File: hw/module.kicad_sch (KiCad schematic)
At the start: 7 parts

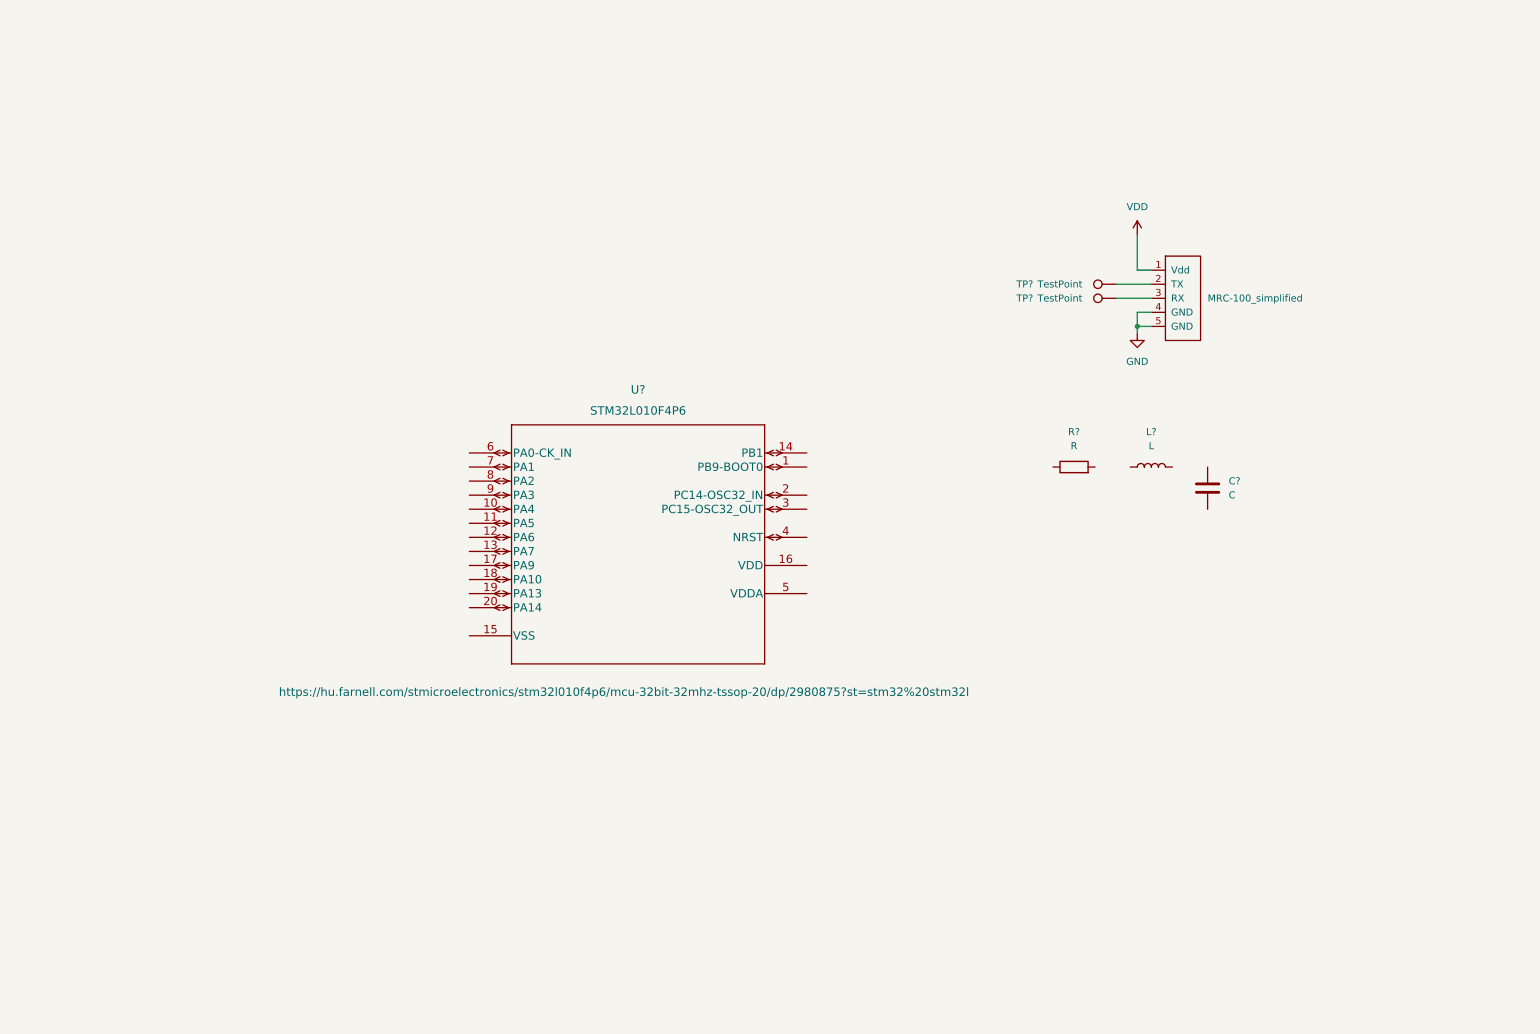
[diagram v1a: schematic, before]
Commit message: added Max919_footprint
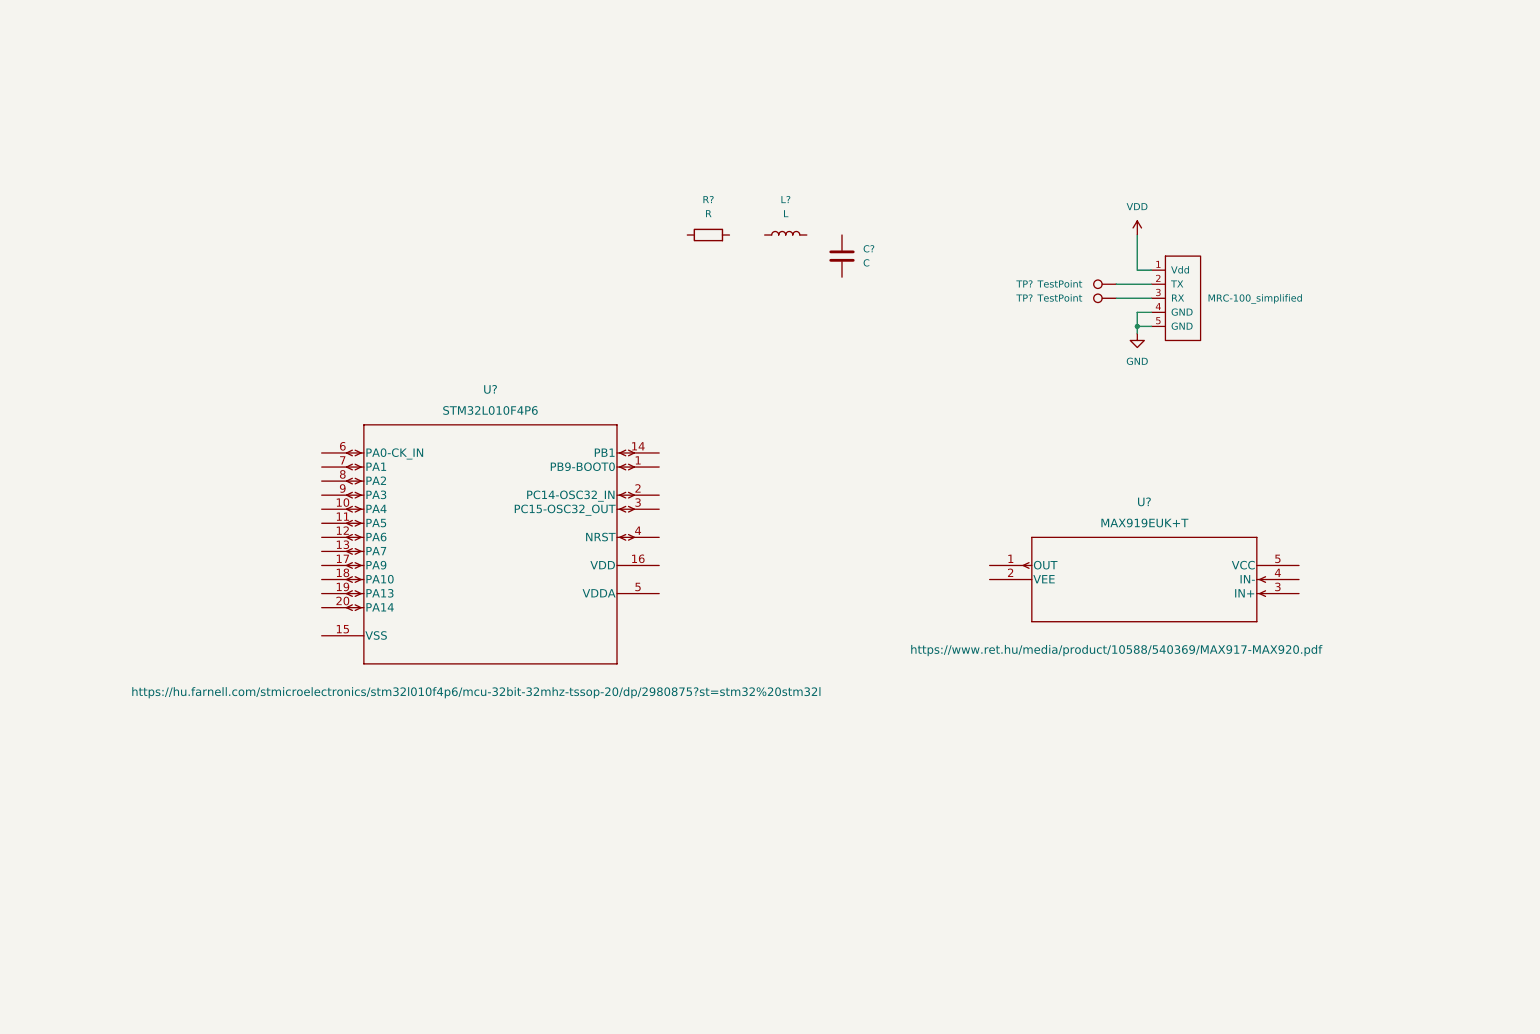
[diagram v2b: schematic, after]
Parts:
- added U?: MAX919EUK+T, max919:MAX919EUK&plus_T, symbol max919:MAX919EUK+T
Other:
- moved on the sheet: C?, L?, R?, U?
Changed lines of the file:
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@@
     (pin "1")
   )
-  (symbol (lib_id "Device:L") (at 210.82 95.25 90) (unit 1)
+  (symbol (lib_id "Device:L") (at 144.78 53.34 90) (unit 1)
     (in_bom yes) (on_board yes) (fields_autoplaced)
-    (property "Reference" "L?" (id 0) (at 210.82 88.9 90))
-    (property "Value" "L" (id 1) (at 210.82 91.44 90))
-    (property "Footprint" "" (id 2) (at 210.82 95.25 0)
+    (property "Reference" "L?" (id 0) (at 144.78 46.99 90))
+    (property "Value" "L" (id 1) (at 144.78 49.53 90))
+    (property "Footprint" "" (id 2) (at 144.78 53.34 0)
       (effects (font (size 1.27 1.27)) hide)
     )
-    (property "Datasheet" "~" (id 3) (at 210.82 95.25 0)
+    (property "Datasheet" "~" (id 3) (at 144.78 53.34 0)
       (effects (font (size 1.27 1.27)) hide)
     )
@@
     (pin "2")
   )
-  (symbol (lib_id "Device:R") (at 196.85 95.25 90) (unit 1)
+  (symbol (lib_id "Device:R") (at 130.81 53.34 90) (unit 1)
     (in_bom yes) (on_board yes) (fields_autoplaced)
-    (property "Reference" "R?" (id 0) (at 196.85 88.9 90))
-    (property "Value" "R" (id 1) (at 196.85 91.44 90))
-    (property "Footprint" "" (id 2) (at 196.85 97.028 90)
+    (property "Reference" "R?" (id 0) (at 130.81 46.99 90))
+    (property "Value" "R" (id 1) (at 130.81 49.53 90))
+    (property "Footprint" "" (id 2) (at 130.81 55.118 90)
       (effects (font (size 1.27 1.27)) hide)
     )
-    (property "Datasheet" "~" (id 3) (at 196.85 95.25 0)
+    (property "Datasheet" "~" (id 3) (at 130.81 53.34 0)
       (effects (font (size 1.27 1.27)) hide)
     )
@@
     (pin "1")
   )
-  (symbol (lib_id "farnell:STM32L010F4P6") (at 87.63 92.71 0) (unit 1)
+  (symbol (lib_id "max919:MAX919EUK+T") (at 181.61 113.03 0) (unit 1)
     (in_bom yes) (on_board yes)
-    (property "Reference" "U?" (id 0) (at 118.11 81.28 0)
+    (property "Reference" "U?" (id 0) (at 209.55 101.6 0)
       (effects (font (size 1.524 1.524)))
     )
-    (property "Value" "STM32L010F4P6" (id 1) (at 118.11 85.09 0)
+    (property "Value" "MAX919EUK+T" (id 1) (at 209.55 105.41 0)
       (effects (font (size 1.524 1.524)))
     )
-    (property "Footprint" "farnell:STM32L010F4P6" (id 2) (at 118.11 86.614 0)
+    (property "Footprint" "max919:MAX919EUK&plus_T" (id 2) (at 209.55 106.934 0)
       (effects (font (size 1.524 1.524)) hide)
     )
-    (property "Datasheet" "https://hu.farnell.com/stmicroelectronics/stm32l010f4p6/mcu-32bit-32mhz-tssop-20/dp/2980875?st=stm32%20stm32l" (id 3) (at 115.57 135.89 0)
+    (property "Datasheet" "https://www.ret.hu/media/product/10588/540369/MAX917-MAX920.pdf" (id 3) (at 204.47 128.27 0)
+      (effects (font (size 1.524 1.524)))
+    )
+    (pin "1")
+    (pin "2")
+    (pin "3")
+    (pin "4")
+    (pin "5")
+  )
+  (symbol (lib_id "farnell:STM32L010F4P6") (at 60.96 92.71 0) (unit 1)
+    (in_bom yes) (on_board yes)
+    (property "Reference" "U?" (id 0) (at 91.44 81.28 0)
+      (effects (font (size 1.524 1.524)))
+    )
+    (property "Value" "STM32L010F4P6" (id 1) (at 91.44 85.09 0)
+      (effects (font (size 1.524 1.524)))
+    )
+    (property "Footprint" "farnell:STM32L010F4P6" (id 2) (at 91.44 86.614 0)
+      (effects (font (size 1.524 1.524)) hide)
+    )
+    (property "Datasheet" "https://hu.farnell.com/stmicroelectronics/stm32l010f4p6/mcu-32bit-32mhz-tssop-20/dp/2980875?st=stm32%20stm32l" (id 3) (at 88.9 135.89 0)
       (effects (font (size 1.524 1.524)))
     )
@@
     (pin "9")
   )
-  (symbol (lib_id "Device:C") (at 220.98 99.06 0) (unit 1)
+  (symbol (lib_id "Device:C") (at 154.94 57.15 0) (unit 1)
     (in_bom yes) (on_board yes) (fields_autoplaced)
-    (property "Reference" "C?" (id 0) (at 224.79 97.7899 0)
+    (property "Reference" "C?" (id 0) (at 158.75 55.8799 0)
       (effects (font (size 1.27 1.27)) (justify left))
     )
-    (property "Value" "C" (id 1) (at 224.79 100.3299 0)
+    (property "Value" "C" (id 1) (at 158.75 58.4199 0)
       (effects (font (size 1.27 1.27)) (justify left))
     )
-    (property "Footprint" "" (id 2) (at 221.9452 102.87 0)
+    (property "Footprint" "" (id 2) (at 155.9052 60.96 0)
       (effects (font (size 1.27 1.27)) hide)
     )
-    (property "Datasheet" "~" (id 3) (at 220.98 99.06 0)
+    (property "Datasheet" "~" (id 3) (at 154.94 57.15 0)
       (effects (font (size 1.27 1.27)) hide)
     )
@@
       (reference "TP?") (unit 1) (value "TestPoint") (footprint "TestPoint:TestPoint_Pad_3.0x3.0mm")
     )
+    (path "/b184c922-aa81-4212-9d5b-fb2052d1a7d8"
+      (reference "U?") (unit 1) (value "MAX919EUK+T") (footprint "max919:MAX919EUK&plus_T")
+    )
     (path "/c3a09ed2-f9ee-4187-a81e-7663ad390909"

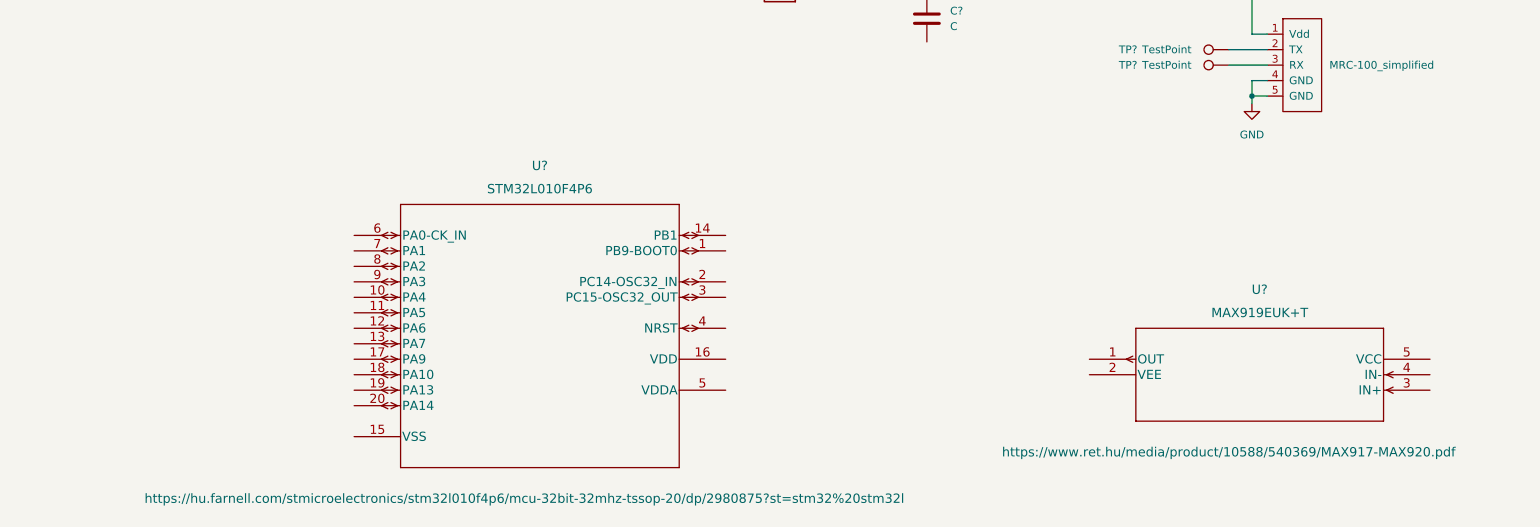
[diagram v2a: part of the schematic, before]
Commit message: Redraw max919 to conventional symbol
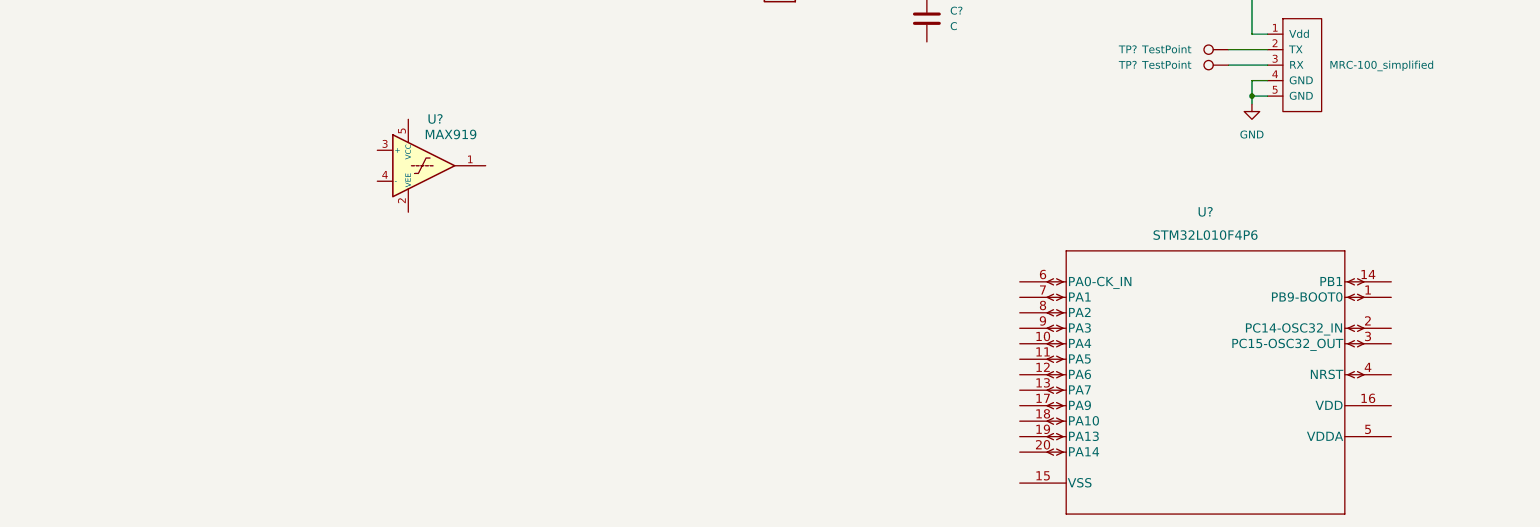
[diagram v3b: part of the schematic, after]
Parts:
- removed U?: MAX919EUK+T, max919:MAX919EUK&plus_T, symbol max919:MAX919EUK+T
- added U?: MAX919, Package_TO_SOT_SMD:SOT-23-5_HandSoldering, symbol RET:MAX919
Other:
- moved on the sheet: U?
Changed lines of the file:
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@@
     (pin "1")
   )
-  (symbol (lib_id "max919:MAX919EUK+T") (at 181.61 113.03 0) (unit 1)
+  (symbol (lib_id "farnell:STM32L010F4P6") (at 170.18 100.33 0) (unit 1)
     (in_bom yes) (on_board yes)
-    (property "Reference" "U?" (id 0) (at 209.55 101.6 0)
+    (property "Reference" "U?" (id 0) (at 200.66 88.9 0)
       (effects (font (size 1.524 1.524)))
     )
-    (property "Value" "MAX919EUK+T" (id 1) (at 209.55 105.41 0)
+    (property "Value" "STM32L010F4P6" (id 1) (at 200.66 92.71 0)
       (effects (font (size 1.524 1.524)))
     )
-    (property "Footprint" "max919:MAX919EUK&plus_T" (id 2) (at 209.55 106.934 0)
+    (property "Footprint" "farnell:STM32L010F4P6" (id 2) (at 200.66 94.234 0)
       (effects (font (size 1.524 1.524)) hide)
     )
-    (property "Datasheet" "https://www.ret.hu/media/product/10588/540369/MAX917-MAX920.pdf" (id 3) (at 204.47 128.27 0)
-      (effects (font (size 1.524 1.524)))
-    )
-    (pin "1")
-    (pin "2")
-    (pin "3")
-    (pin "4")
-    (pin "5")
-  )
-  (symbol (lib_id "farnell:STM32L010F4P6") (at 60.96 92.71 0) (unit 1)
-    (in_bom yes) (on_board yes)
-    (property "Reference" "U?" (id 0) (at 91.44 81.28 0)
-      (effects (font (size 1.524 1.524)))
-    )
-    (property "Value" "STM32L010F4P6" (id 1) (at 91.44 85.09 0)
-      (effects (font (size 1.524 1.524)))
-    )
-    (property "Footprint" "farnell:STM32L010F4P6" (id 2) (at 91.44 86.614 0)
+    (property "Datasheet" "https://hu.farnell.com/stmicroelectronics/stm32l010f4p6/mcu-32bit-32mhz-tssop-20/dp/2980875?st=stm32%20stm32l" (id 3) (at 198.12 143.51 0)
       (effects (font (size 1.524 1.524)) hide)
-    )
-    (property "Datasheet" "https://hu.farnell.com/stmicroelectronics/stm32l010f4p6/mcu-32bit-32mhz-tssop-20/dp/2980875?st=stm32%20stm32l" (id 3) (at 88.9 135.89 0)
-      (effects (font (size 1.524 1.524)))
     )
     (pin "1")
@@
     (pin "2")
   )
+  (symbol (lib_id "RET:MAX919") (at 71.12 81.28 0) (unit 1)
+    (in_bom yes) (on_board yes)
+    (property "Reference" "U?" (id 0) (at 74.295 73.66 0)
+      (effects (font (size 1.524 1.524)))
+    )
+    (property "Value" "MAX919" (id 1) (at 76.835 76.2 0)
+      (effects (font (size 1.524 1.524)))
+    )
+    (property "Footprint" "Package_TO_SOT_SMD:SOT-23-5_HandSoldering" (id 2) (at 81.28 77.47 0)
+      (effects (font (size 1.524 1.524)) hide)
+    )
+    (property "Datasheet" "https://www.ret.hu/media/product/10588/540369/MAX917-MAX920.pdf" (id 3) (at 82.55 92.71 0)
+      (effects (font (size 1.524 1.524)) hide)
+    )
+    (pin "1")
+    (pin "2")
+    (pin "3")
+    (pin "4")
+    (pin "5")
+  )
   (sheet_instances
     (path "/" (page "1"))
@@
       (reference "TP?") (unit 1) (value "TestPoint") (footprint "TestPoint:TestPoint_Pad_3.0x3.0mm")
     )
-    (path "/b184c922-aa81-4212-9d5b-fb2052d1a7d8"
-      (reference "U?") (unit 1) (value "MAX919EUK+T") (footprint "max919:MAX919EUK&plus_T")
-    )
     (path "/c3a09ed2-f9ee-4187-a81e-7663ad390909"
       (reference "U?") (unit 1) (value "STM32L010F4P6") (footprint "farnell:STM32L010F4P6")
     )
+    (path "/ee709747-fe1d-4f49-8562-b9f2cf862921"
+      (reference "U?") (unit 1) (value "MAX919") (footprint "Package_TO_SOT_SMD:SOT-23-5_HandSoldering")
+    )
   )
